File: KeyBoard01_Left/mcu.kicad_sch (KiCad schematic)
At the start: 1 part

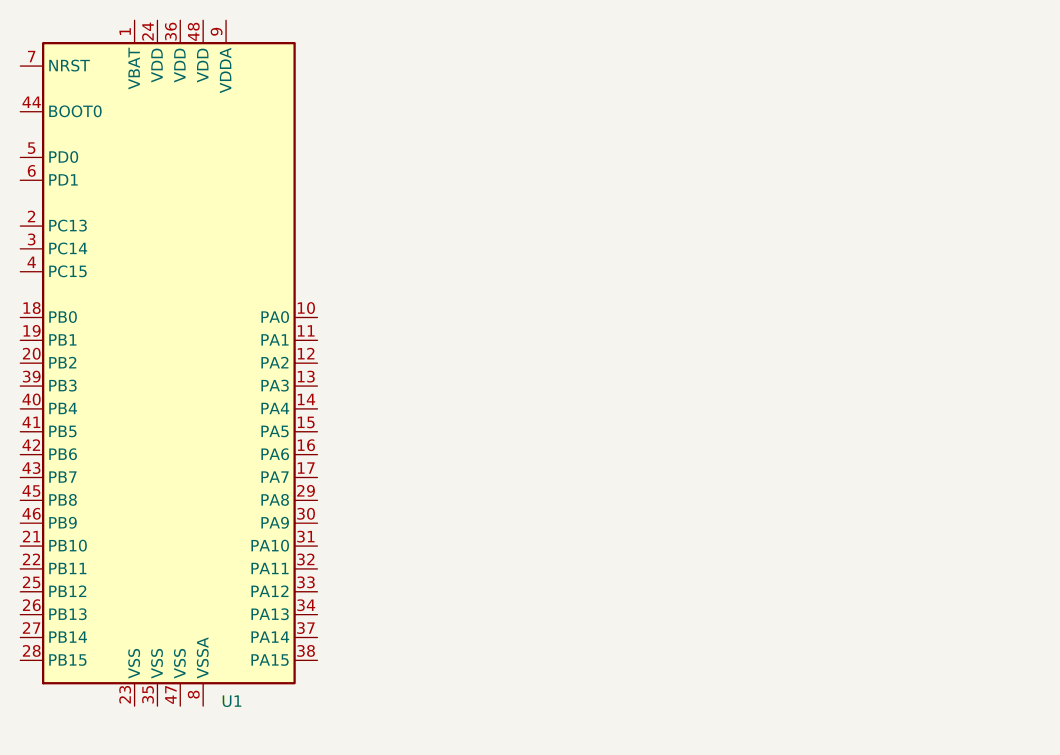
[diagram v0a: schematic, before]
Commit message: SCH MCU: add 10 pin JTAG connector
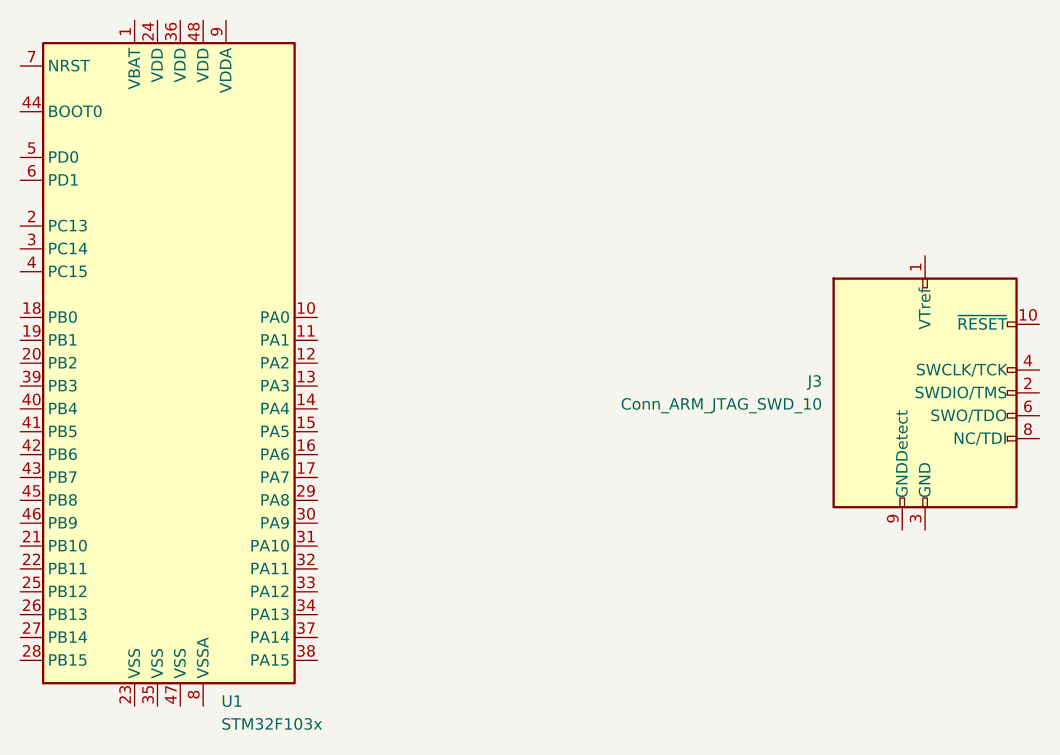
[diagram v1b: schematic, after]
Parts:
- added J3: Conn_ARM_JTAG_SWD_10, symbol Connector:Conn_ARM_JTAG_SWD_10
- U1: value ~ -> STM32F103x
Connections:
- new net: J3.3 (GND), J3.5 (GND)
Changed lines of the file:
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@@
-(kicad_sch (version 20211123) (generator eeschema)
+(kicad_sch (version 20230121) (generator eeschema)
   (paper "A4")
   (symbol (lib_id "MCU_ST_STM32F1:STM32F103C8Tx") (at 144.5768 94.488 0) (unit 1)
-    (in_bom yes) (on_board yes) (fields_autoplaced)
-    (property "Reference" "U1" (id 0) (at 149.1362 132.08 0)
+    (in_bom yes) (on_board yes) (dnp no) (fields_autoplaced)
+    (property "Reference" "U1" (at 149.1362 132.08 0)
       (effects (font (size 1.27 1.27)) (justify left))
     )
-    (property "Value" "~" (id 1) (at 149.1362 134.62 0)
+    (property "Value" "STM32F103x" (at 149.1362 134.62 0)
       (effects (font (size 1.27 1.27)) (justify left))
     )
-    (property "Footprint" "" (id 2) (at 129.3368 130.048 0)
+    (property "Footprint" "" (at 129.3368 130.048 0)
       (effects (font (size 1.27 1.27)) (justify right) hide)
     )
-    (property "Datasheet" "http://www.st.com/st-web-ui/static/active/en/resource/technical/document/datasheet/CD00161566.pdf" (id 3) (at 144.5768 94.488 0)
+    (property "Datasheet" "http://www.st.com/st-web-ui/static/active/en/resource/technical/document/datasheet/CD00161566.pdf" (at 144.5768 94.488 0)
       (effects (font (size 1.27 1.27)) hide)
     )
@@
     (pin "8")
     (pin "9")
+    (instances
+      (project "KeyBoard01_Left"
+        (path "/30001e54-b931-4c99-a85a-cc67ed27d667/3eed219e-ef44-46a2-a482-b7191acccc64"
+          (reference "U1") (unit 1)
+        )
+      )
+    )
+  )
+  (symbol (lib_id "Connector:Conn_ARM_JTAG_SWD_10") (at 227.33 97.79 0) (unit 1)
+    (in_bom yes) (on_board yes) (dnp no) (fields_autoplaced)
+    (property "Reference" "J3" (at 215.9 96.52 0)
+      (effects (font (size 1.27 1.27)) (justify right))
+    )
+    (property "Value" "Conn_ARM_JTAG_SWD_10" (at 215.9 99.06 0)
+      (effects (font (size 1.27 1.27)) (justify right))
+    )
+    (property "Footprint" "" (at 227.33 97.79 0)
+      (effects (font (size 1.27 1.27)) hide)
+    )
+    (property "Datasheet" "http://infocenter.arm.com/help/topic/com.arm.doc.ddi0314h/DDI0314H_coresight_components_trm.pdf" (at 218.44 129.54 90)
+      (effects (font (size 1.27 1.27)) hide)
+    )
+    (pin "4")
+    (pin "8")
+    (pin "9")
+    (pin "10")
+    (pin "6")
+    (pin "3")
+    (pin "5")
+    (pin "2")
+    (pin "1")
+    (pin "7")
+    (instances
+      (project "KeyBoard01_Left"
+        (path "/30001e54-b931-4c99-a85a-cc67ed27d667/3eed219e-ef44-46a2-a482-b7191acccc64"
+          (reference "J3") (unit 1)
+        )
+      )
+    )
   )
 )

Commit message: SCH: modify MCU sheet
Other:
- company: (none) -> Embedded Dojo
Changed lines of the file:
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@@
 (kicad_sch (version 20230121) (generator eeschema)
   (paper "A4")
+  (title_block
+    (company "Embedded Dojo")
+    (comment 1 "imuguruza and hans")
+  )
   (symbol (lib_id "MCU_ST_STM32F1:STM32F103C8Tx") (at 144.5768 94.488 0) (unit 1)
     (in_bom yes) (on_board yes) (dnp no) (fields_autoplaced)
